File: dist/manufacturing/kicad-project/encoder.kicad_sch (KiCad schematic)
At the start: 9 parts, among them U18 AS5047P-ATSM

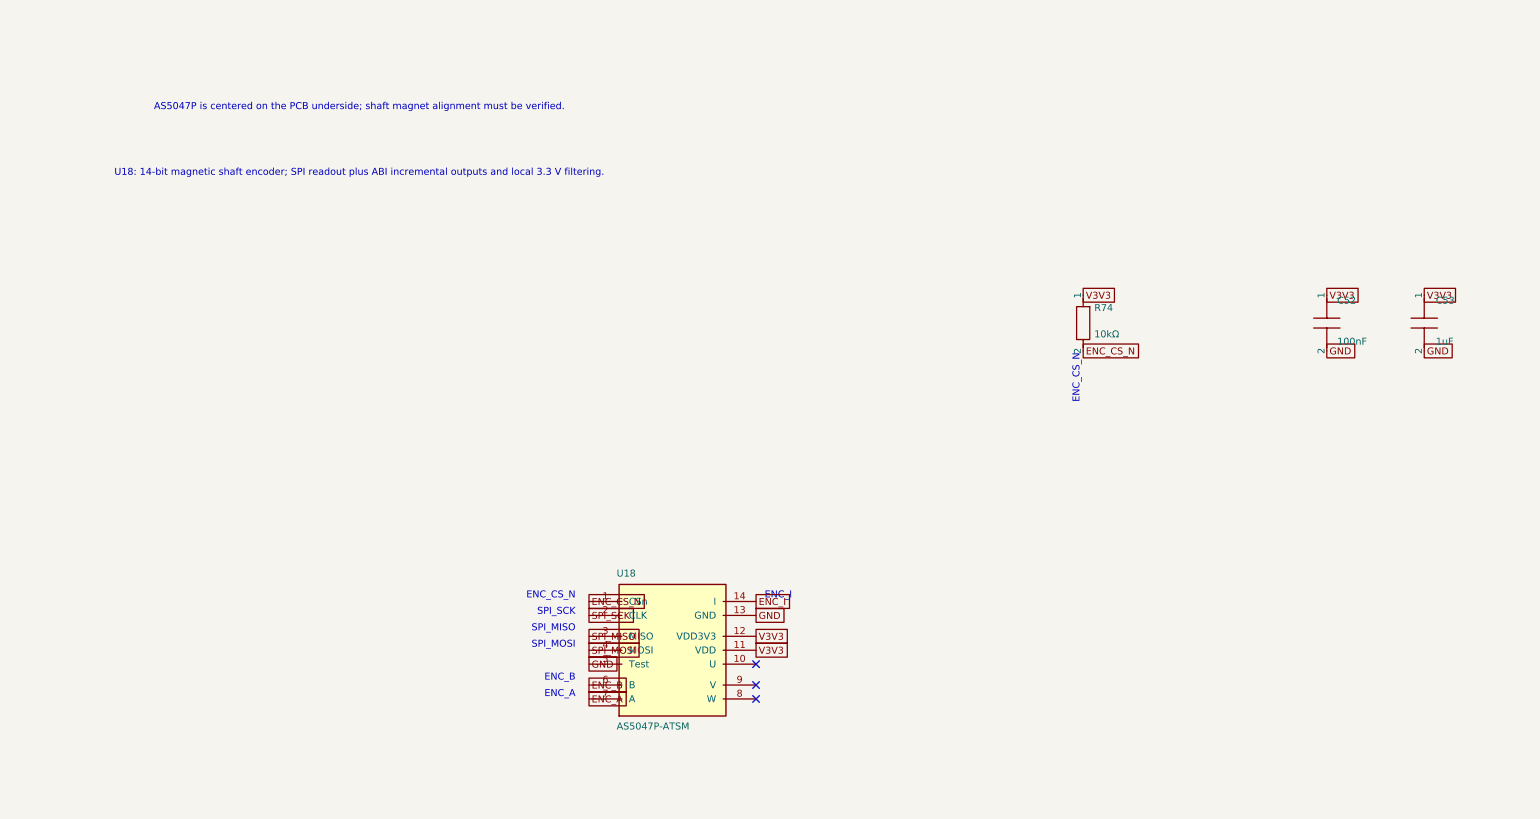
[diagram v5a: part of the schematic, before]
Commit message: Make centered encoder optional and specify the JST motor harness
Place U18 and its local capacitors on bottom as DNP, exclude them from
fitted BOM/CPL and paste, and reroute their connections. Keep all fitted
parts on top and preserve the motor, power, USB and mounting geometry.

Document NEMA17/NEMA23 references, the VH mating cable and connector
purposes. Refresh native checks and manufacturing/review artifacts.
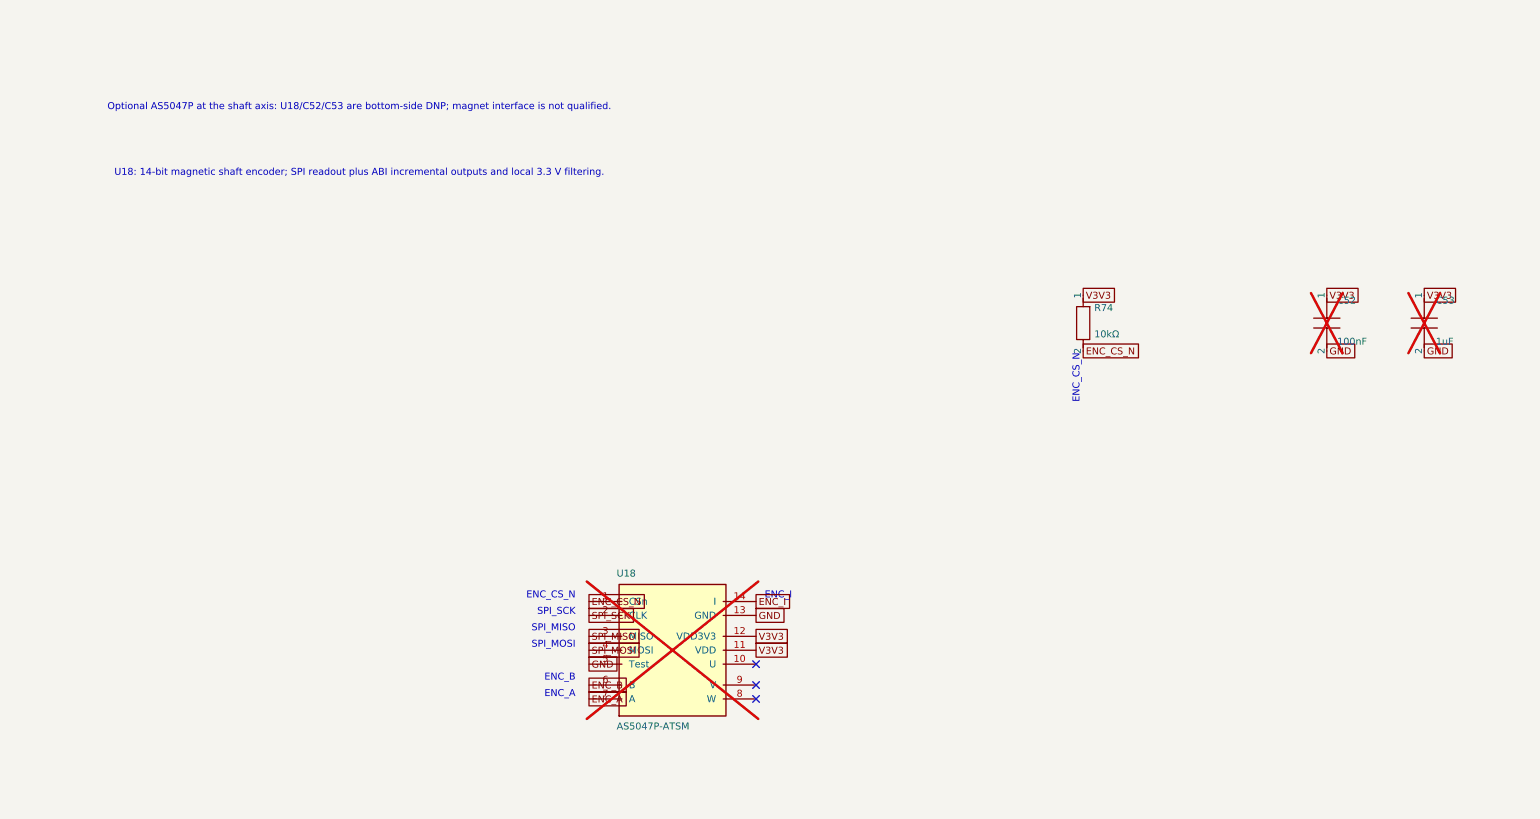
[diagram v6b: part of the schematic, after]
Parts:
- C52, C53, U18: now not fitted; now left out of the parts list
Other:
- note added: "Optional AS5047P at the shaft axis: U18/C52/C53 are bottom-side DNP; magnet interface is not qualified."
- note removed: "AS5047P is centered on the PCB underside; shaft magnet alignment must be verified."
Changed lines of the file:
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@@
     (unit 1)
     (exclude_from_sim no)
-    (in_bom yes)
-    (on_board yes)
-    (dnp no)
+    (in_bom no)
+    (on_board yes)
+    (dnp yes)
     (fields_autoplaced no)
     (property "Reference" "U18"
@@
     (instances
       (project ""
-        (path "/102a6df3-4bbe-4fc6-82a4-9e4a7af263ed/c5791791-b136-439a-a690-108a2021c28b"
+        (path "/76c36cad-99be-409a-bafe-984536be09f8/31c67d5e-f3de-4ea7-ab6f-da16448a0614"
           (reference "U18")
           (unit 1)
@@
     (instances
       (project ""
-        (path "/102a6df3-4bbe-4fc6-82a4-9e4a7af263ed/c5791791-b136-439a-a690-108a2021c28b"
+        (path "/76c36cad-99be-409a-bafe-984536be09f8/31c67d5e-f3de-4ea7-ab6f-da16448a0614"
           (reference "R74")
           (unit 1)
@@
     (unit 1)
     (exclude_from_sim no)
-    (in_bom yes)
-    (on_board yes)
-    (dnp no)
+    (in_bom no)
+    (on_board yes)
+    (dnp yes)
     (fields_autoplaced no)
     (property "Reference" "C52"
@@
     (instances
       (project ""
-        (path "/102a6df3-4bbe-4fc6-82a4-9e4a7af263ed/c5791791-b136-439a-a690-108a2021c28b"
+        (path "/76c36cad-99be-409a-bafe-984536be09f8/31c67d5e-f3de-4ea7-ab6f-da16448a0614"
           (reference "C52")
           (unit 1)
@@
     (unit 1)
     (exclude_from_sim no)
-    (in_bom yes)
-    (on_board yes)
-    (dnp no)
+    (in_bom no)
+    (on_board yes)
+    (dnp yes)
     (fields_autoplaced no)
     (property "Reference" "C53"
@@
     (instances
       (project ""
-        (path "/102a6df3-4bbe-4fc6-82a4-9e4a7af263ed/c5791791-b136-439a-a690-108a2021c28b"
+        (path "/76c36cad-99be-409a-bafe-984536be09f8/31c67d5e-f3de-4ea7-ab6f-da16448a0614"
           (reference "C53")
           (unit 1)
@@
     (instances
       (project ""
-        (path "/102a6df3-4bbe-4fc6-82a4-9e4a7af263ed/c5791791-b136-439a-a690-108a2021c28b"
+        (path "/76c36cad-99be-409a-bafe-984536be09f8/31c67d5e-f3de-4ea7-ab6f-da16448a0614"
           (reference "TP_ENC_3V3")
           (unit 1)
@@
     (instances
       (project ""
-        (path "/102a6df3-4bbe-4fc6-82a4-9e4a7af263ed/c5791791-b136-439a-a690-108a2021c28b"
+        (path "/76c36cad-99be-409a-bafe-984536be09f8/31c67d5e-f3de-4ea7-ab6f-da16448a0614"
           (reference "TP_ENC_A")
           (unit 1)
@@
     (instances
       (project ""
-        (path "/102a6df3-4bbe-4fc6-82a4-9e4a7af263ed/c5791791-b136-439a-a690-108a2021c28b"
+        (path "/76c36cad-99be-409a-bafe-984536be09f8/31c67d5e-f3de-4ea7-ab6f-da16448a0614"
           (reference "TP_ENC_B")
           (unit 1)
@@
     (instances
       (project ""
-        (path "/102a6df3-4bbe-4fc6-82a4-9e4a7af263ed/c5791791-b136-439a-a690-108a2021c28b"
+        (path "/76c36cad-99be-409a-bafe-984536be09f8/31c67d5e-f3de-4ea7-ab6f-da16448a0614"
           (reference "TP_ENC_I")
           (unit 1)
@@
     (instances
       (project ""
-        (path "/102a6df3-4bbe-4fc6-82a4-9e4a7af263ed/c5791791-b136-439a-a690-108a2021c28b"
+        (path "/76c36cad-99be-409a-bafe-984536be09f8/31c67d5e-f3de-4ea7-ab6f-da16448a0614"
           (reference "TP_ENC_GND")
           (unit 1)
@@
     )
   )
-  (text "AS5047P is centered on the PCB underside; shaft magnet alignment must be verified."
+  (text "Optional AS5047P at the shaft axis: U18/C52/C53 are bottom-side DNP; magnet interface is not qualified."
     (at 3.81375000000002 54.5925 0)
     (effects

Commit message: Fix source warnings and organize schematic on A4 sheets
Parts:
- TP_ENC_3V3, TP_ENC_A, TP_ENC_B, TP_ENC_GND, TP_ENC_I: now not fitted; now left out of the parts list
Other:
- note added: "14 / Optional Shaft Encoder"
- note added: "SPI plus ABI test access; magnet interface for the ordered single-shaft motor is unqualified."
- note added: "U18 AS5047P and C52/C53 are centered bottom-side DNP footprints."
- note removed: "09 / Shaft Encoder and Monitor"
- note removed: "Optional AS5047P at the shaft axis: U18/C52/C53 are bottom-side DNP; magnet interface is not qualified."
- note removed: "U18: 14-bit magnetic shaft encoder; SPI readout plus ABI incremental outputs and local 3.3 V filtering."
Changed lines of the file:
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@@
     (property "Value" "AS5047P-ATSM"
       (id 1)
-      (at 50.763750000000016 167.5425 0)
+      (at 50.763750000000016 167.54250000000002 0)
       (effects
         (font
@@
     (instances
       (project ""
-        (path "/888afcaf-aca0-4ec5-ab90-6fb77de6f3f5/dc6eeaa8-f19c-4360-a56c-d8a9ce4cb79d"
+        (path "/9ce6d0ce-044d-4e77-ac59-1290d960b5b5/1c5e474b-d84b-4f5b-b328-942a63906b28"
           (reference "U18")
           (unit 1)
@@
     (instances
       (project ""
-        (path "/888afcaf-aca0-4ec5-ab90-6fb77de6f3f5/dc6eeaa8-f19c-4360-a56c-d8a9ce4cb79d"
+        (path "/9ce6d0ce-044d-4e77-ac59-1290d960b5b5/1c5e474b-d84b-4f5b-b328-942a63906b28"
           (reference "R74")
           (unit 1)
@@
     (property "Reference" "C52"
       (id 0)
-      (at 182.23875000000004 90.5925 0)
+      (at 182.23875 90.5925 0)
       (effects
         (font
@@
     (property "Value" "100nF"
       (id 1)
-      (at 182.23875000000004 96.5925 0)
+      (at 182.23875 96.5925 0)
       (effects
         (font
@@
     (instances
       (project ""
-        (path "/888afcaf-aca0-4ec5-ab90-6fb77de6f3f5/dc6eeaa8-f19c-4360-a56c-d8a9ce4cb79d"
+        (path "/9ce6d0ce-044d-4e77-ac59-1290d960b5b5/1c5e474b-d84b-4f5b-b328-942a63906b28"
           (reference "C52")
           (unit 1)
@@
     (instances
       (project ""
-        (path "/888afcaf-aca0-4ec5-ab90-6fb77de6f3f5/dc6eeaa8-f19c-4360-a56c-d8a9ce4cb79d"
+        (path "/9ce6d0ce-044d-4e77-ac59-1290d960b5b5/1c5e474b-d84b-4f5b-b328-942a63906b28"
           (reference "C53")
           (unit 1)
@@
     (unit 1)
     (exclude_from_sim no)
-    (in_bom yes)
+    (in_bom no)
     (on_board yes)
-    (dnp no)
+    (dnp yes)
     (fields_autoplaced no)
     (property "Reference" "TP_ENC_3V3"
@@
     (instances
       (project ""
-        (path "/888afcaf-aca0-4ec5-ab90-6fb77de6f3f5/dc6eeaa8-f19c-4360-a56c-d8a9ce4cb79d"
+        (path "/9ce6d0ce-044d-4e77-ac59-1290d960b5b5/1c5e474b-d84b-4f5b-b328-942a63906b28"
           (reference "TP_ENC_3V3")
           (unit 1)
@@
     (unit 1)
     (exclude_from_sim no)
-    (in_bom yes)
+    (in_bom no)
     (on_board yes)
-    (dnp no)
+    (dnp yes)
     (fields_autoplaced no)
     (property "Reference" "TP_ENC_A"
@@
     (instances
       (project ""
-        (path "/888afcaf-aca0-4ec5-ab90-6fb77de6f3f5/dc6eeaa8-f19c-4360-a56c-d8a9ce4cb79d"
+        (path "/9ce6d0ce-044d-4e77-ac59-1290d960b5b5/1c5e474b-d84b-4f5b-b328-942a63906b28"
           (reference "TP_ENC_A")
           (unit 1)
@@
     (unit 1)
     (exclude_from_sim no)
-    (in_bom yes)
+    (in_bom no)
     (on_board yes)
-    (dnp no)
+    (dnp yes)
     (fields_autoplaced no)
     (property "Reference" "TP_ENC_B"
@@
     (instances
       (project ""
-        (path "/888afcaf-aca0-4ec5-ab90-6fb77de6f3f5/dc6eeaa8-f19c-4360-a56c-d8a9ce4cb79d"
+        (path "/9ce6d0ce-044d-4e77-ac59-1290d960b5b5/1c5e474b-d84b-4f5b-b328-942a63906b28"
           (reference "TP_ENC_B")
           (unit 1)
@@
     (unit 1)
     (exclude_from_sim no)
-    (in_bom yes)
+    (in_bom no)
     (on_board yes)
-    (dnp no)
+    (dnp yes)
     (fields_autoplaced no)
     (property "Reference" "TP_ENC_I"
@@
     (instances
       (project ""
-        (path "/888afcaf-aca0-4ec5-ab90-6fb77de6f3f5/dc6eeaa8-f19c-4360-a56c-d8a9ce4cb79d"
+        (path "/9ce6d0ce-044d-4e77-ac59-1290d960b5b5/1c5e474b-d84b-4f5b-b328-942a63906b28"
           (reference "TP_ENC_I")
           (unit 1)
@@
     (unit 1)
     (exclude_from_sim no)
-    (in_bom yes)
+    (in_bom no)
     (on_board yes)
-    (dnp no)
+    (dnp yes)
     (fields_autoplaced no)
     (property "Reference" "TP_ENC_GND"
@@
     (instances
       (project ""
-        (path "/888afcaf-aca0-4ec5-ab90-6fb77de6f3f5/dc6eeaa8-f19c-4360-a56c-d8a9ce4cb79d"
+        (path "/9ce6d0ce-044d-4e77-ac59-1290d960b5b5/1c5e474b-d84b-4f5b-b328-942a63906b28"
           (reference "TP_ENC_GND")
           (unit 1)
@@
     )
   )
-  (text "09 / Shaft Encoder and Monitor"
-    (at 3.81375000000002 33.5925 0)
-    (effects
-      (font
-        (size 1.27 1.27)
-        (color 0 0 0 1)
-      )
-    )
-  )
-  (text "Optional AS5047P at the shaft axis: U18/C52/C53 are bottom-side DNP; magnet interface is not qualified."
-    (at 3.81375000000002 54.5925 0)
-    (effects
-      (font
-        (size 1.27 1.27)
-        (color 0 0 0 1)
-      )
-    )
-  )
-  (text "U18: 14-bit magnetic shaft encoder; SPI readout plus ABI incremental outputs and local 3.3 V filtering."
-    (at 3.81375000000002 66.5925 0)
+  (text "14 / Optional Shaft Encoder"
+    (at 228.81375000000003 -8.407499999999999 0)
+    (effects
+      (font
+        (size 1.27 1.27)
+        (color 0 0 0 1)
+      )
+    )
+  )
+  (text "U18 AS5047P and C52/C53 are centered bottom-side DNP footprints."
+    (at 228.81375000000003 9.592500000000001 0)
+    (effects
+      (font
+        (size 1.27 1.27)
+        (color 0 0 0 1)
+      )
+    )
+  )
+  (text "SPI plus ABI test access; magnet interface for the ordered single-shaft motor is unqualified."
+    (at 228.81375000000003 20.0925 0)
     (effects
       (font
@@
   )
   (text "ENC_CS_N"
-    (at 43.263750000000016 143.6925 0)
+    (at 43.26374999999999 143.6925 0)
     (effects
       (font
@@
   )
   (text "SPI_MISO"
-    (at 43.263750000000016 149.6925 0)
+    (at 43.26374999999999 149.6925 0)
     (effects
       (font
@@
   )
   (text "SPI_MOSI"
-    (at 43.263750000000016 152.6925 0)
+    (at 43.26374999999999 152.6925 0)
     (effects
       (font
@@
   )
   (text "ENC_B"
-    (at 386.01375 182.6925 0)
+    (at 386.0137500000001 182.6925 0)
     (effects
       (font
@@
   )
   (text "ENC_I"
-    (at 273.5137500000001 209.6925 0)
-    (effects
-      (font
+    (at 273.51375 209.6925 0)
+    (effects
+      (font
